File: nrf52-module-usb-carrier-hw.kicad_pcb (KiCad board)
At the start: 2 copper layers, 38.1 x 50.8 mm, 43 parts, among them J1 USB_C_Receptacle_USB2.0_16P, J2 Conn_ARM_JTAG_SWD_10, U1 XC6206PxxxMR, U2 USBLC6-2SC6, U3 CH340N, U4 E73-2G4M04S1B, U5 LSM6DSO, U6 W25Q128JVS, U7 LIS3MDL

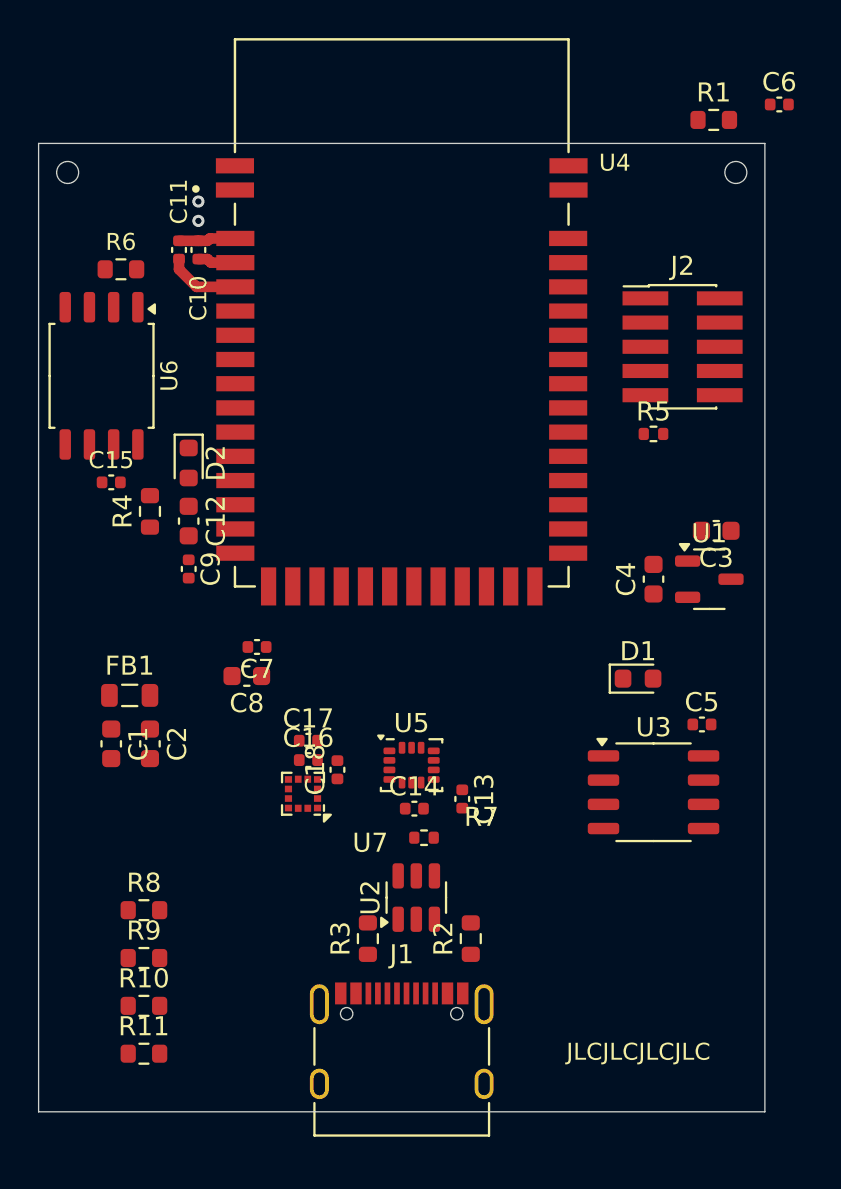
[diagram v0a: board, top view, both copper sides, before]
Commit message: Routed diff pairs, IMU sensors, SPI Flash
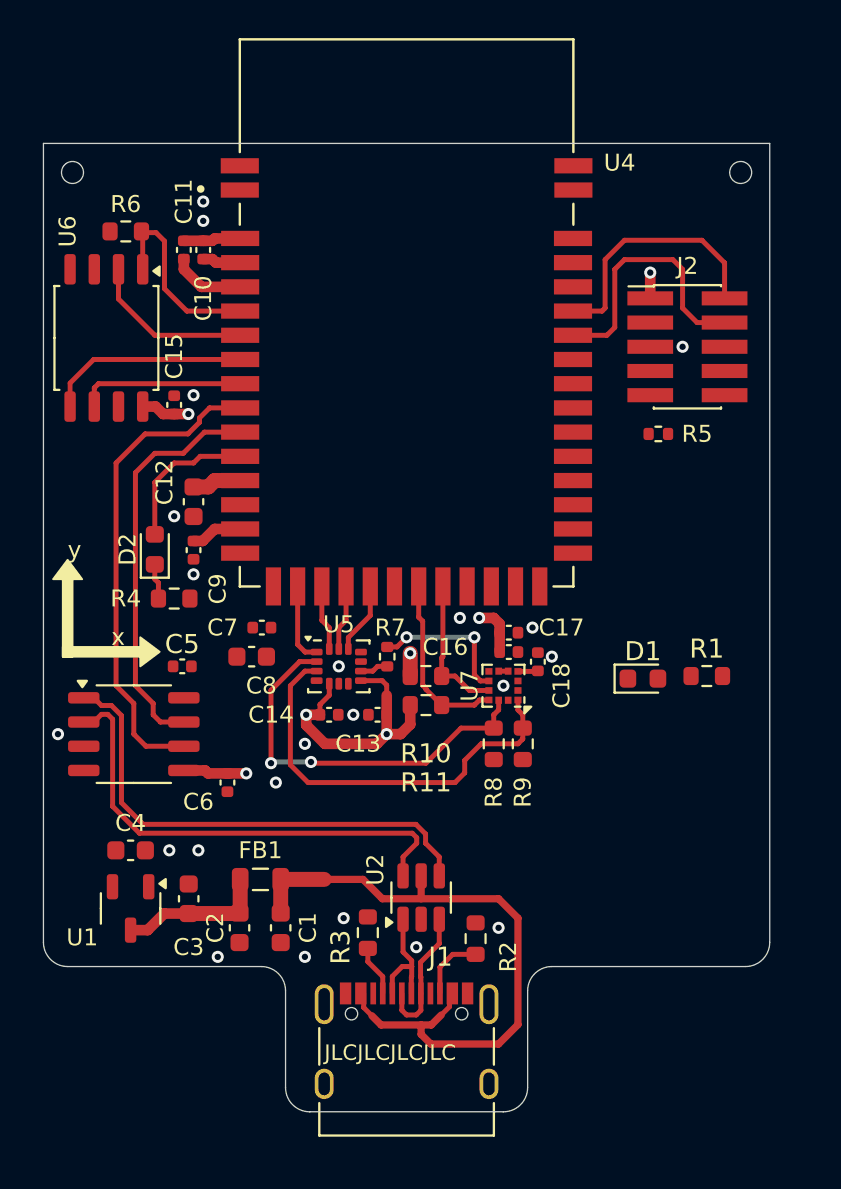
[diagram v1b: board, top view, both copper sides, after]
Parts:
- moved C6 45.9 mm to (99.1, 92.5), turned to -90 degrees
- moved U1 34.9 mm to (94.0, 99.1), turned to -90 degrees
- moved C3 33.7 mm to (97.0, 98.6), turned to 90 degrees
- moved C4 30.9 mm to (94.0, 96.0), turned to 0 degrees
- moved R1 29.2 mm to (124.2, 86.9)
- moved C5 27.4 mm to (96.7, 86.4)
- moved U3 27.4 mm to (94.1, 89.9)
- moved R11 24.7 mm to (109.5, 86.9), turned to 180 degrees
- moved R9 22.8 mm to (114.6, 90.4), turned to 90 degrees
- moved R10 21.6 mm to (109.5, 88.4)
- moved R8 20.3 mm to (113.0, 90.4), turned to 90 degrees
- moved C1 13.1 mm to (101.9, 100.1)
- moved C16 11.9 mm to (113.8, 85.6)
- moved C17 11.9 mm to (113.8, 84.6)
- moved C18 11.9 mm to (115.3, 86.1)
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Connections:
- net /Power + MCU + SWD/SWCLK renamed /Power + MCU + SWD/SWDCLK
- U4 pad 10: unconnected-(U4-P0.30-Pad10) -> /Power + MCU + SWD/UART_TX
- U4 pad 30: /Power + MCU + SWD/UART_RX -> unconnected-(U4-P0.15-Pad30)
- U4 pad 31: /Power + MCU + SWD/UART_TX -> unconnected-(U4-P0.16-Pad31)
- U4 pad 9: unconnected-(U4-P0.29-Pad9) -> /Power + MCU + SWD/UART_RX
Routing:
- net VBUS: track 0.00 -> 35.4 mm
- net /Power + MCU + SWD/USB_DP: track 0.00 -> 26.1 mm
- net /Power + MCU + SWD/UART_RX: track 0.00 -> 25.3 mm
- net /Power + MCU + SWD/USB_DN: track 0.00 -> 25.3 mm
- net +3V3: track 0.00 -> 24.8 mm, vias 0 -> 6
- net /Peripherals/MAG_SCLK: track 0.00 -> 21.9 mm
- net /Power + MCU + SWD/UART_TX: track 0.00 -> 21.2 mm
- net /Peripherals/MAG_SDA_MOSI: track 0.00 -> 20.9 mm, vias 0 -> 2
- net /Power + MCU + SWD/SWDCLK: track 0.00 -> 13.9 mm
- net /Power + MCU + SWD/SWDIO: track 0.00 -> 13.3 mm
- net FLASH_nCS: track 0.00 -> 10.7 mm
- net FLASH_MOSI: track 0.00 -> 10.7 mm
- net MAG_nCHIP_SEL: track 0.00 -> 9.31 mm
- net FLASH_MISO: track 0.00 -> 8.73 mm
- net FLASH_SCLK: track 0.00 -> 8.72 mm
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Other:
- outline, holes or cut-outs redrawn
- board text added: "x"
- board text added: "y"

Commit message: Added an I2C IO expander, plus 2 pushbuttons and  2 LEDs controlled by the expander
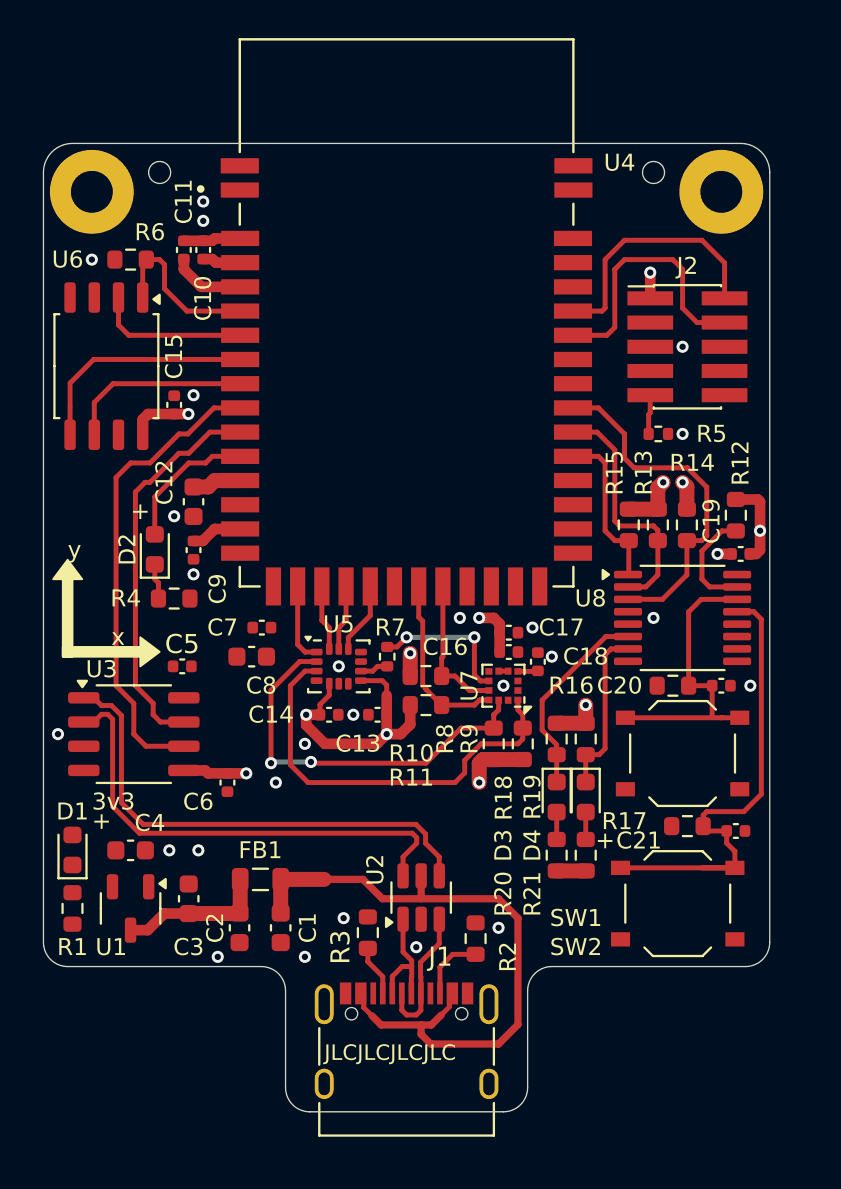
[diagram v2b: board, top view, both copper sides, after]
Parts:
- added C19: 100nF, Capacitor_SMD:C_0402_1005Metric, F.Cu at (126.0, 80.5)
- added C20: 100nF, Capacitor_SMD:C_0402_1005Metric, F.Cu at (125.0, 87.4)
- added C21: 100nF, Capacitor_SMD:C_0402_1005Metric, F.Cu at (125.7, 95.0)
- added D3: 19-217/GHC-YR1S2/6T, LED_SMD:LED_0603_1608Metric, F.Cu at (116.3, 93.2)
- added D4: 19-217/GHC-YR1S2/6T, LED_SMD:LED_0603_1608Metric, F.Cu at (117.9, 93.2)
- added H3: MountingHole_Pad, MountingHole:MountingHole_2.2mm_M2_Pad, F.Cu at (91.9, 61.5)
- added H4: MountingHole_Pad, MountingHole:MountingHole_2.2mm_M2_Pad, F.Cu at (125.0, 61.5)
- added R12: 5k1, Resistor_SMD:R_0603_1608Metric, F.Cu at (125.7, 78.4)
- added R13: 5k1, Resistor_SMD:R_0603_1608Metric, F.Cu at (121.6, 78.9)
- added R14: 5k1, Resistor_SMD:R_0603_1608Metric, F.Cu at (123.2, 78.9)
- added R15: 5k1, Resistor_SMD:R_0603_1608Metric, F.Cu at (120.1, 78.9)
- added R16: 5k1, Resistor_SMD:R_0603_1608Metric, F.Cu at (122.4, 87.4)
- added R17: 5k1, Resistor_SMD:R_0603_1608Metric, F.Cu at (123.2, 94.7)
- added R18: 5k1, Resistor_SMD:R_0603_1608Metric, F.Cu at (116.3, 90.2)
- added R19: 5k1, Resistor_SMD:R_0603_1608Metric, F.Cu at (117.9, 90.2)
- added R20: 1k, Resistor_SMD:R_0603_1608Metric, F.Cu at (116.3, 96.3)
- added R21: 1k, Resistor_SMD:R_0603_1608Metric, F.Cu at (117.9, 96.3)
- added SW1: SW_Push, Button_Switch_SMD:SW_Push_1P1T_XKB_TS-1187A, F.Cu at (122.9, 90.9)
- added SW2: SW_Push, Button_Switch_SMD:SW_Push_1P1T_XKB_TS-1187A, F.Cu at (122.7, 98.8)
- added U8: PCA9557PW, Package_SO:TSSOP-16_4.4x5mm_P0.65mm, F.Cu at (122.9, 83.8)
- moved R1 35.4 mm to (90.9, 99.1), turned to 90 degrees
- moved D1 31.2 mm to (90.9, 96.0), turned to 90 degrees
- moved H1 4.57 mm to (95.5, 60.5)
- moved H2 4.57 mm to (121.4, 60.5)
- moved R6 1.50 mm to (94.0, 65.0)
- moved U6 1.48 mm to (92.7, 70.6)
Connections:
- U4 pad 32: unconnected-(U4-P0.17-Pad32) -> EXPANDER_SDA
- U4 pad 33: unconnected-(U4-P0.18-Pad33) -> EXPANDER_SCL
- U4 pad 34: unconnected-(U4-P0.19-Pad34) -> EXPANDER_A0
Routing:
- net /Peripherals/IO6_SW_HIGH: track 0.00 -> 25.5 mm
- net EXPANDER_A0: track 0.00 -> 18.6 mm
- net +3V3: track 24.8 -> 40.5 mm, vias 6 -> 12
- net /Peripherals/IO7_SW_HIGH: track 0.00 -> 15.6 mm
- net EXPANDER_SCL: track 0.00 -> 12.9 mm
- net /Peripherals/IO0_LED_C: track 0.00 -> 10.5 mm
- net /Peripherals/IO1_LED_C: track 0.00 -> 8.84 mm
- net EXPANDER_SDA: track 0.00 -> 8.58 mm
- net /Peripherals/EXPANDER_nRESET: track 0.00 -> 5.46 mm
- net GND: track 4.20 -> 6.44 mm, vias 23 -> 27
- net FLASH_nCS: track 10.7 -> 8.58 mm
- net /Power + MCU + SWD/SWD_GND_DET: track 0.00 -> 2.07 mm
- net FLASH_MOSI: track 10.7 -> 12.1 mm
- net /Peripherals/IO1_LED_A: track 0.00 -> 1.44 mm
- net /Peripherals/IO0_LED_A: track 0.00 -> 1.44 mm
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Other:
- outline, holes or cut-outs redrawn
- board text added: "+"
- board text added: "3v3"

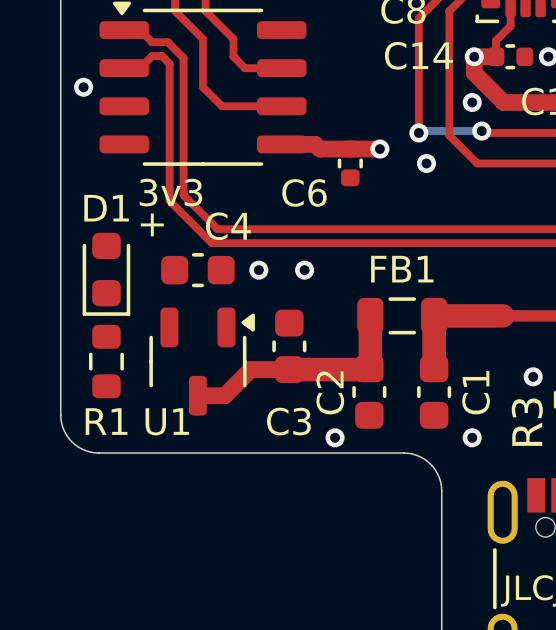
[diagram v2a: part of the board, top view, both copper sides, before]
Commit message: PWR and GND netclass cleanup
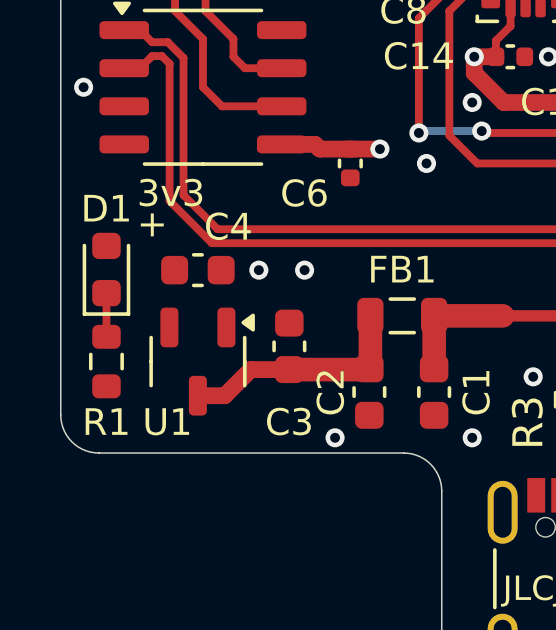
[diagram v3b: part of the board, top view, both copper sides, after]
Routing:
- net /Power + MCU + SWD/PWR_LED_C: track 0.00 -> 1.46 mm
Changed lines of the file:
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@@
+	)
+	(segment
+		(start 90.932 96.7795)
+		(end 90.932 98.235)
+		(width 0.261112)
+		(layer "F.Cu")
+		(net 11)
 	)
 	(segment

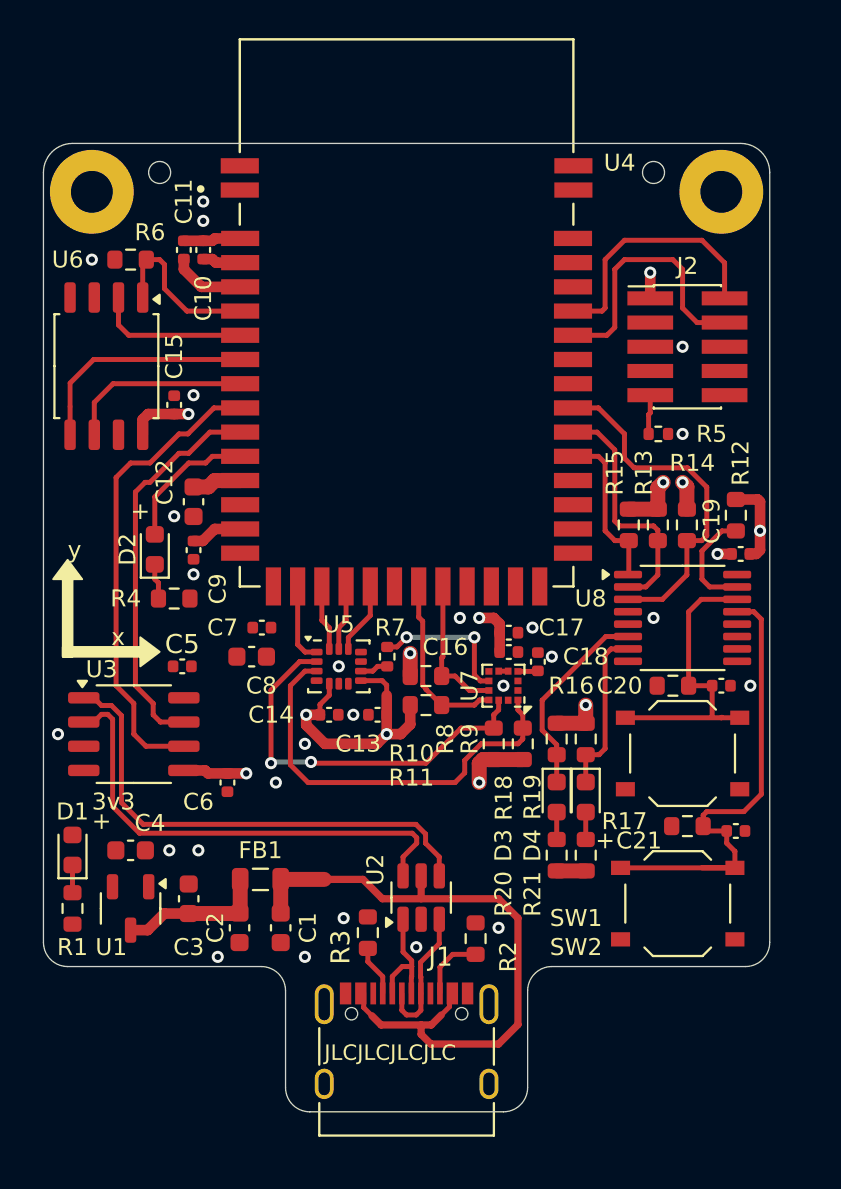
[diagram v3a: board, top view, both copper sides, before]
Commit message: Started routing power
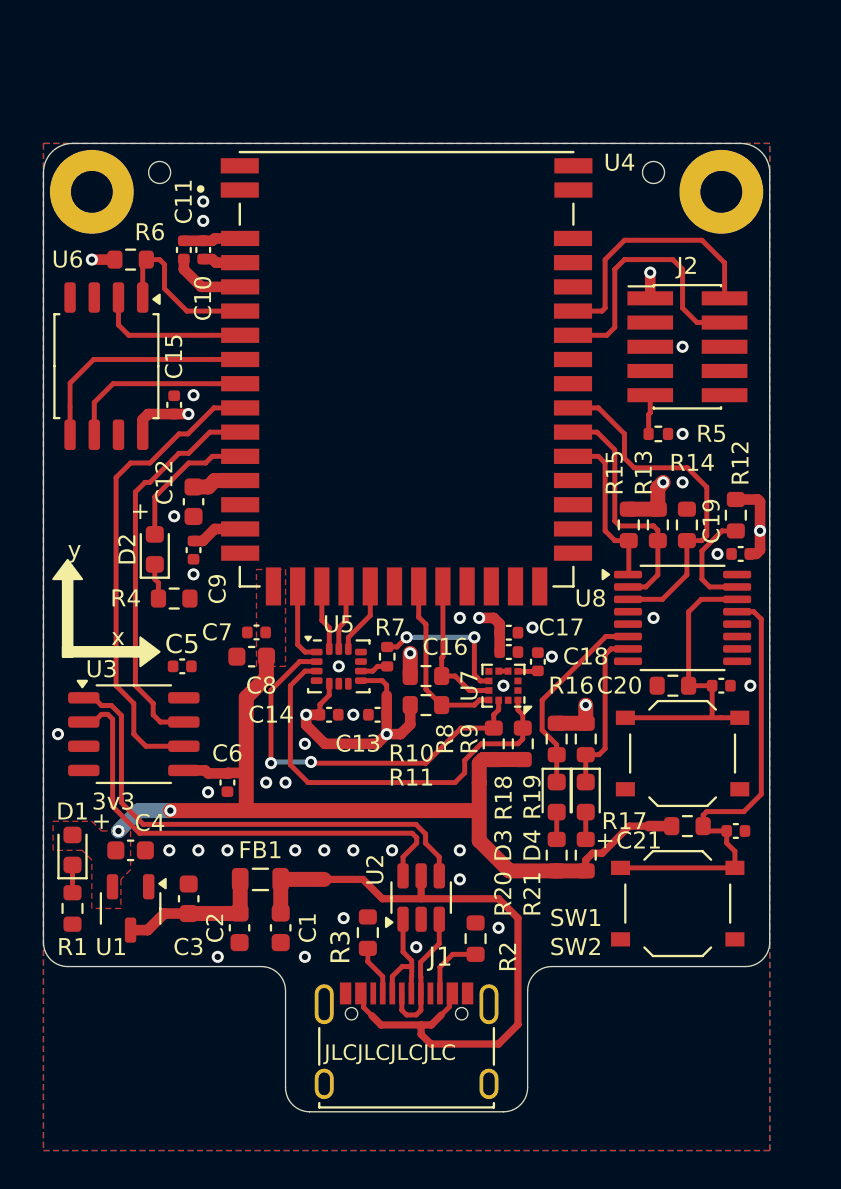
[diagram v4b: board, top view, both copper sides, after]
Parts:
- moved C7 0.38 mm to (100.6, 84.6)
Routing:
- net +3V3: track 40.5 -> 83.1 mm, vias 12 -> 11
- net GND: track 6.44 -> 4.20 mm, vias 27 -> 37
- net /Peripherals/IO6_SW_HIGH: track 25.5 -> 23.8 mm
- net VBUS: track 35.4 -> 34.8 mm
- added copper zone on F.Cu, net +3V3
- added copper zone on B.Cu, net GND
- added copper zone on F.Cu, net GND

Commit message: Updated PCB file to handle DRC.  No errors, few warnings remaining
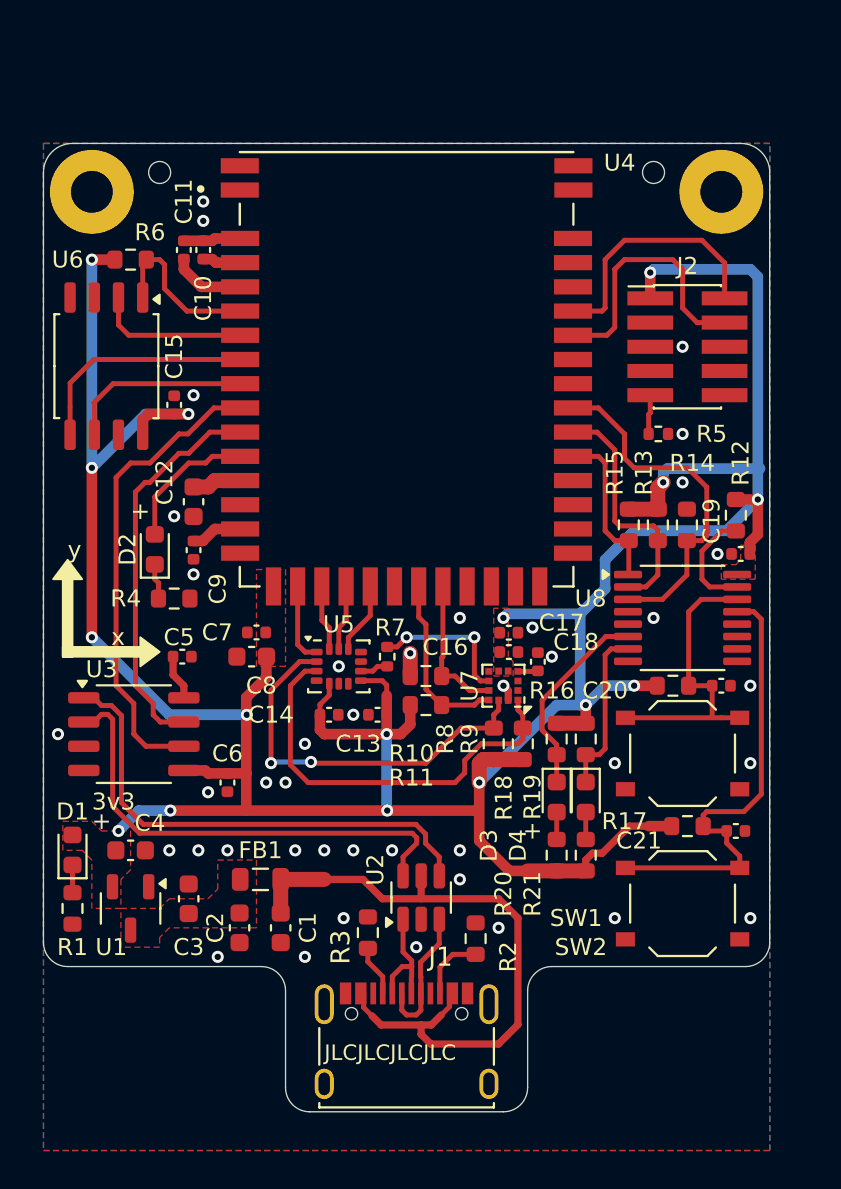
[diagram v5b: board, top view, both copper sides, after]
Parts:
- moved C5 0.51 mm to (96.7, 85.9)
- moved SW2 0.25 mm to (122.9, 98.8)
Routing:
- net +3V3: track 83.1 -> 174.1 mm, vias 11 -> 16
- net +5V: track 7.78 -> 0.00 mm
- net /Power + MCU + SWD/V3: track 0.00 -> 2.39 mm
- net GND: track 4.20 -> 5.06 mm, vias 37 -> 41
- added copper zone on F.Cu, net +5V

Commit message: Cleaned up schematic with comments from datasheets.  Added stitching vias to PCB
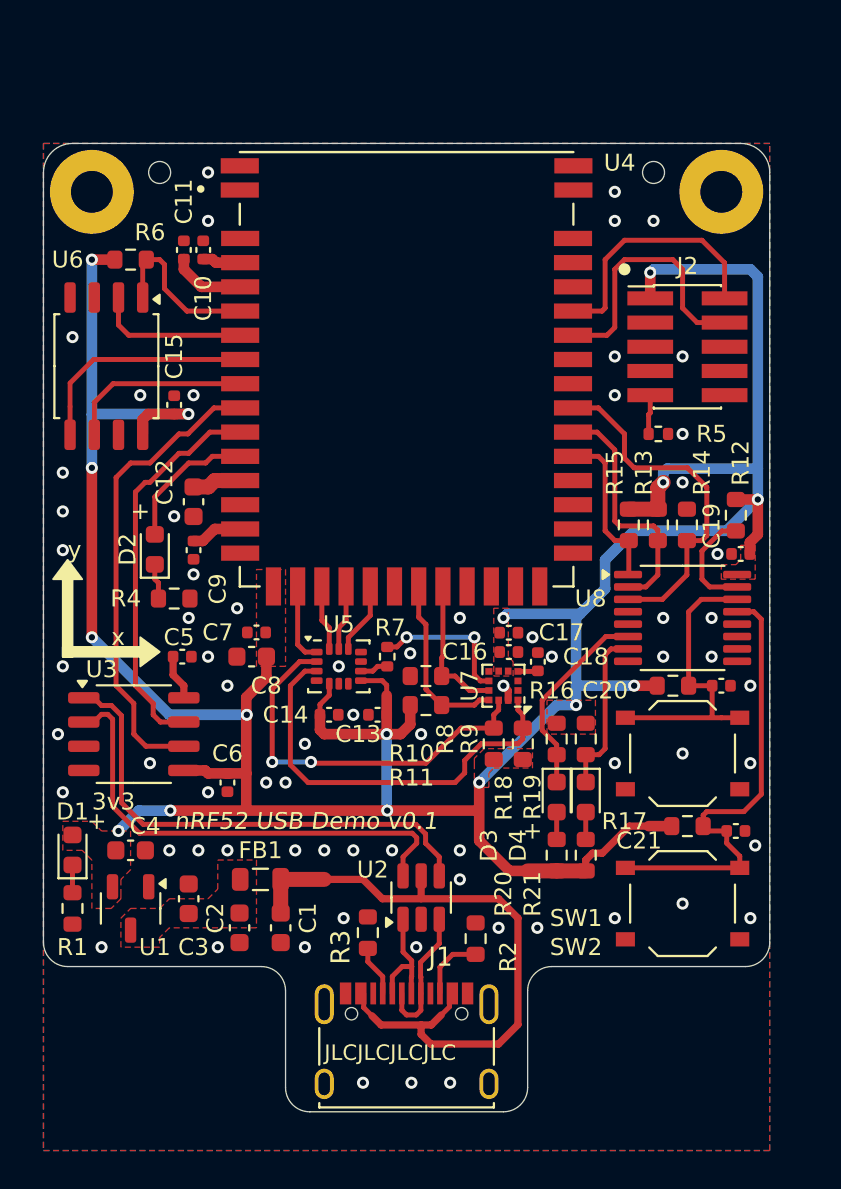
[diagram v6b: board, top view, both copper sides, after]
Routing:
- net +3V3: track 174.1 -> 166.6 mm
- net GND: track 5.06 -> 0.87 mm, vias 41 -> 70
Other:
- board text added: "nRF52 USB Demo v0.1"
